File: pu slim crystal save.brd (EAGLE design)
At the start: 18.7 x 54.6 mm, 24 parts, among them U1 ATMEGA328P-PU, X1 87758-0216

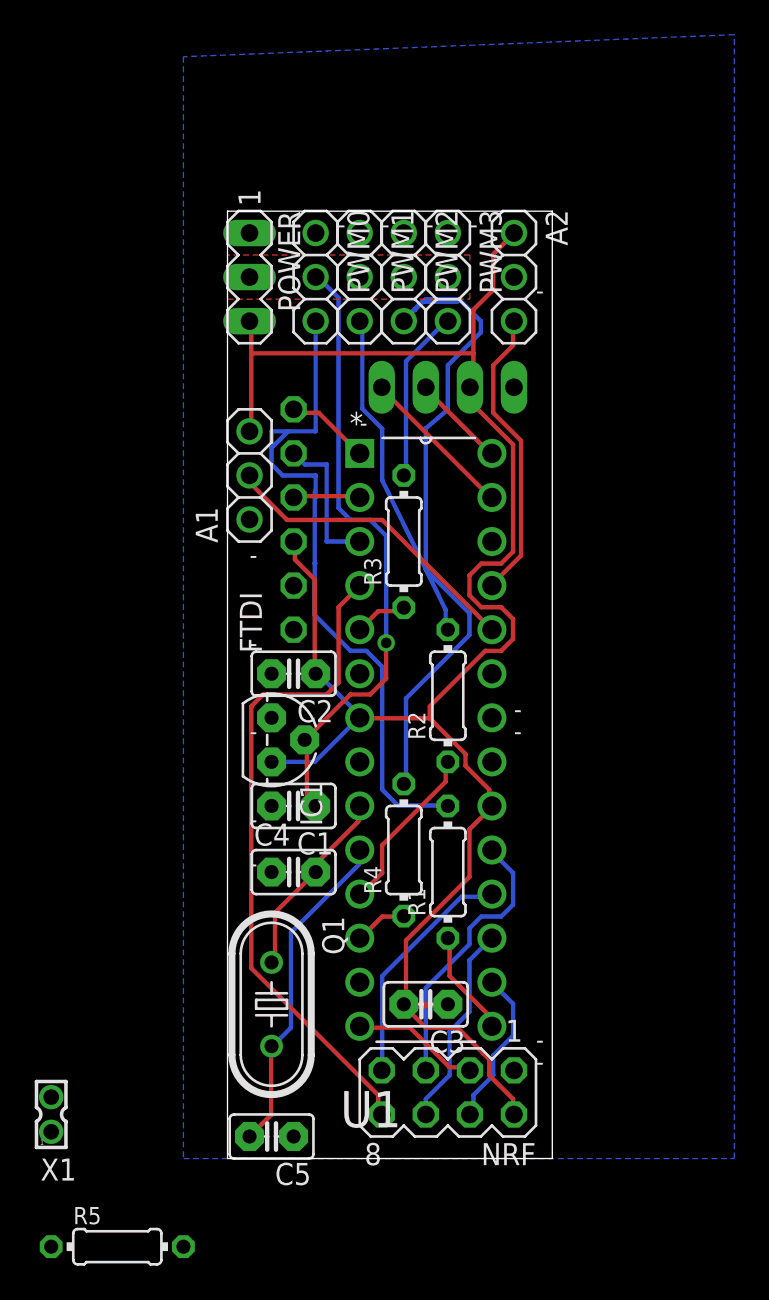
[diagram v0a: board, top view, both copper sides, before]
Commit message: added status led on d7
digital only. with resistor
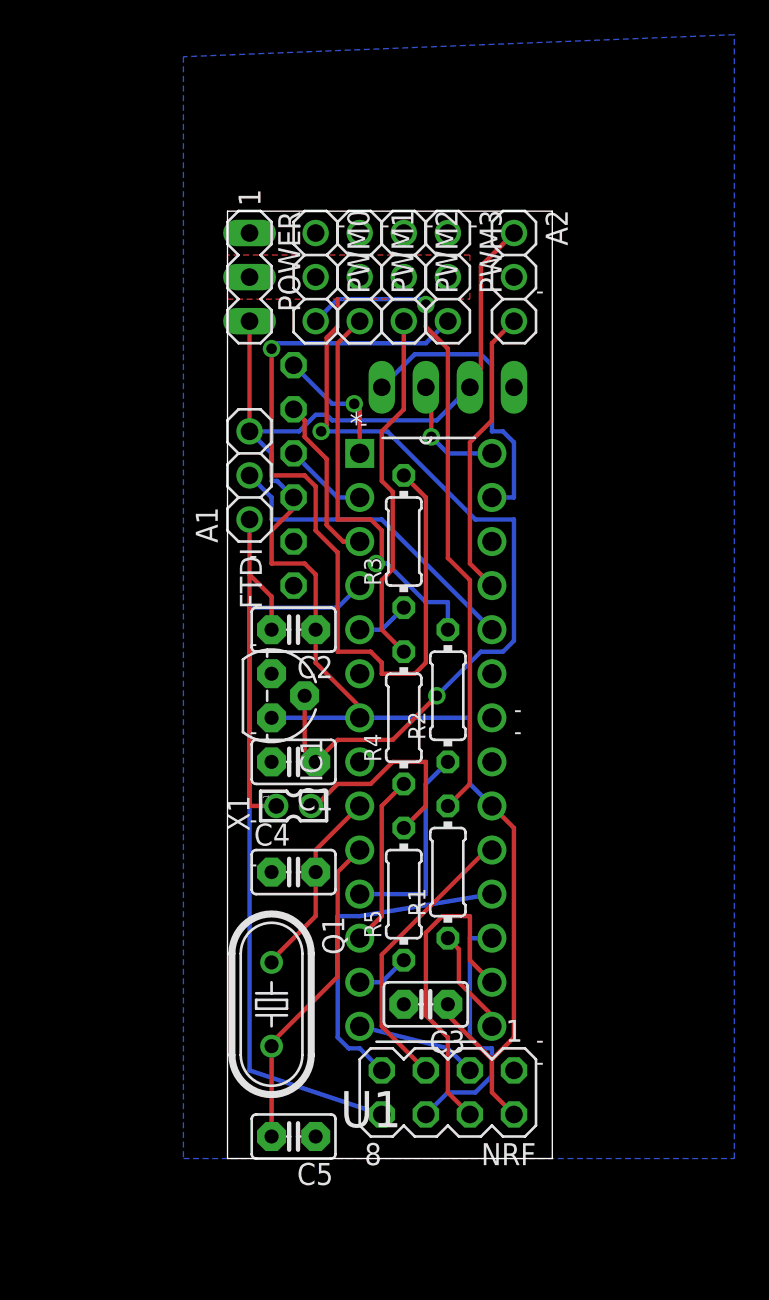
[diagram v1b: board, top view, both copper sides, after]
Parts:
- moved R5 26.2 mm to (10.2, 15.2), turned to 90 degrees
- moved X1 22.6 mm to (3.81, 20.3), turned to 270 degrees
- moved R4 7.62 mm to (10.2, 25.4)
- moved IC1 2.54 mm to (2.54, 26.7)
- moved C1 2.54 mm to (3.81, 22.9)
- moved C2 2.54 mm to (3.81, 30.5)
- moved FTDI 2.54 mm to (3.81, 39.4)
- moved C5 1.27 mm to (3.81, 1.27)
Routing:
- net PWM3OUT: track 9.98 -> 48.5 mm, vias 0 -> 1
- net GND: track 0.00 -> 21.8 mm
- net VCC: track 111.9 -> 92.4 mm
- net PWM2OUT: track 39.1 -> 20.6 mm
- net 7: track 0.00 -> 12.0 mm
- net VIN: track 35.8 -> 46.6 mm, vias 1 -> 2
- net 10PWM: track 9.15 -> 18.8 mm
- net SDA: track 9.00 -> 17.2 mm
- net 6PWM: track 3.05 -> 9.94 mm
- net MISO: track 13.7 -> 19.3 mm
- net PWM1OUT: track 19.3 -> 23.4 mm, vias 0 -> 1
- net D2: track 38.3 -> 41.6 mm
- net MOSI: track 11.7 -> 14.8 mm
- net D7: track 0.00 -> 3.07 mm
- net RST: track 4.91 -> 7.40 mm, vias 0 -> 1
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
